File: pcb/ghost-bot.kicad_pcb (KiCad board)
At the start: 2 copper layers, 111 x 60 mm, 39 parts, among them J1 Conn_01x03_Pin, J2 Conn_01x03_Pin, J3 Conn_01x04_Pin, J4 Conn_01x02_Pin, J5 Conn_01x05_Pin, J6 Conn_01x04_Pin, SW1 SW_Push, SW2 SW_Push, SW3 Switch

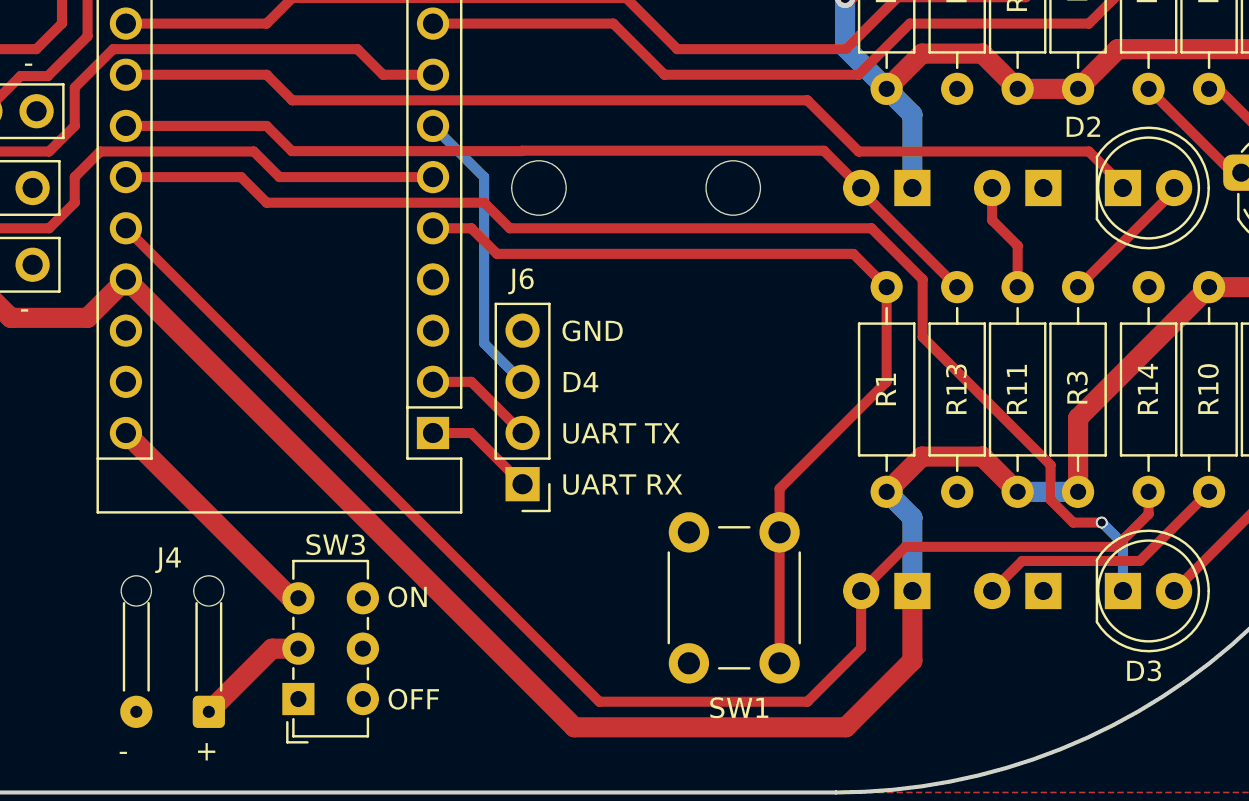
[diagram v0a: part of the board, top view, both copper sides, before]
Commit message: Issue: Fix LED1 pin:  Attempted to swap A5 and A6 in schematic and PCB (although not sure what I may of broken in the mean time).
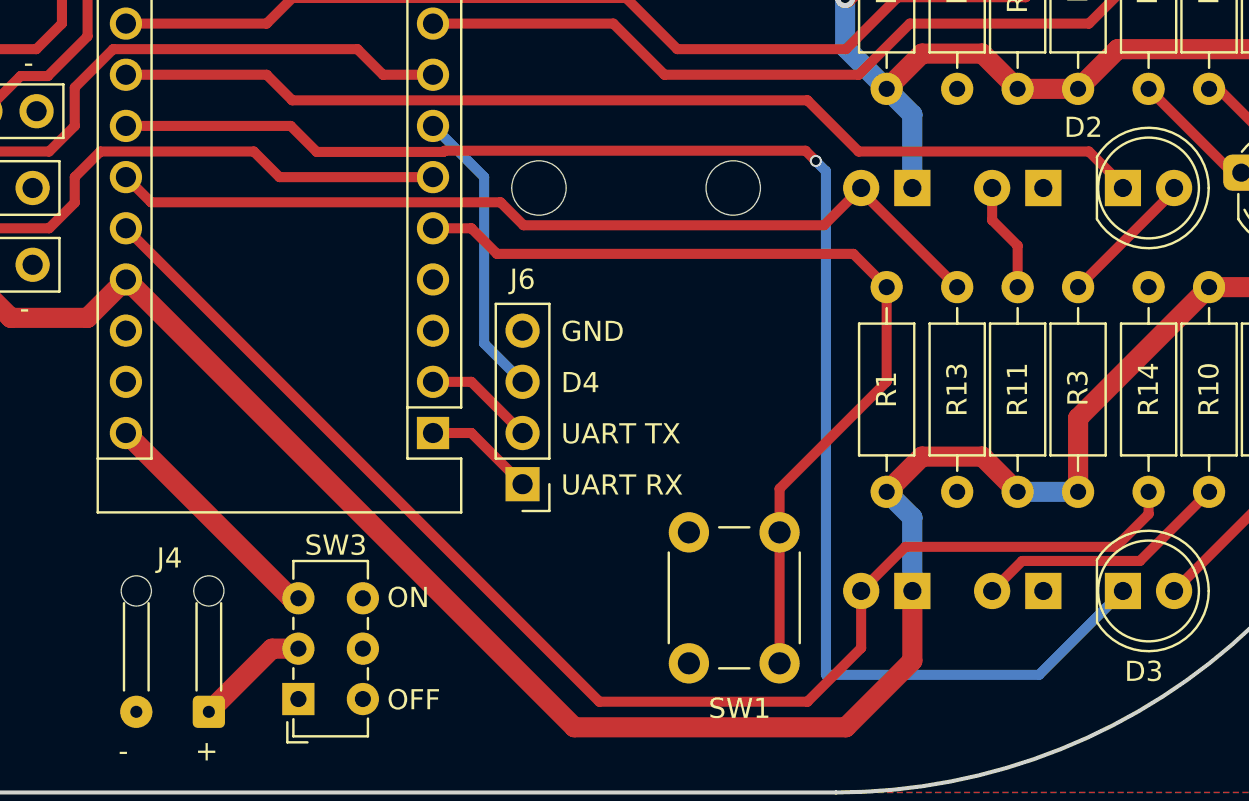
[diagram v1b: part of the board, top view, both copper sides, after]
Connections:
- A1 pad 24: /PD1 -> /LED1
- A1 pad 25: /LED1 -> /PD1
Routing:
- net /LED1: track 62.1 -> 77.2 mm
